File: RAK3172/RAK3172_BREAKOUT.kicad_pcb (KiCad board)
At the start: 2 copper layers, 29.4 x 36.8 mm, 5 parts, among them J1 Conn_01x14_Male, J2 Conn_01x14_Male, J3 Conn_01x14_Male, U1 RAK3172

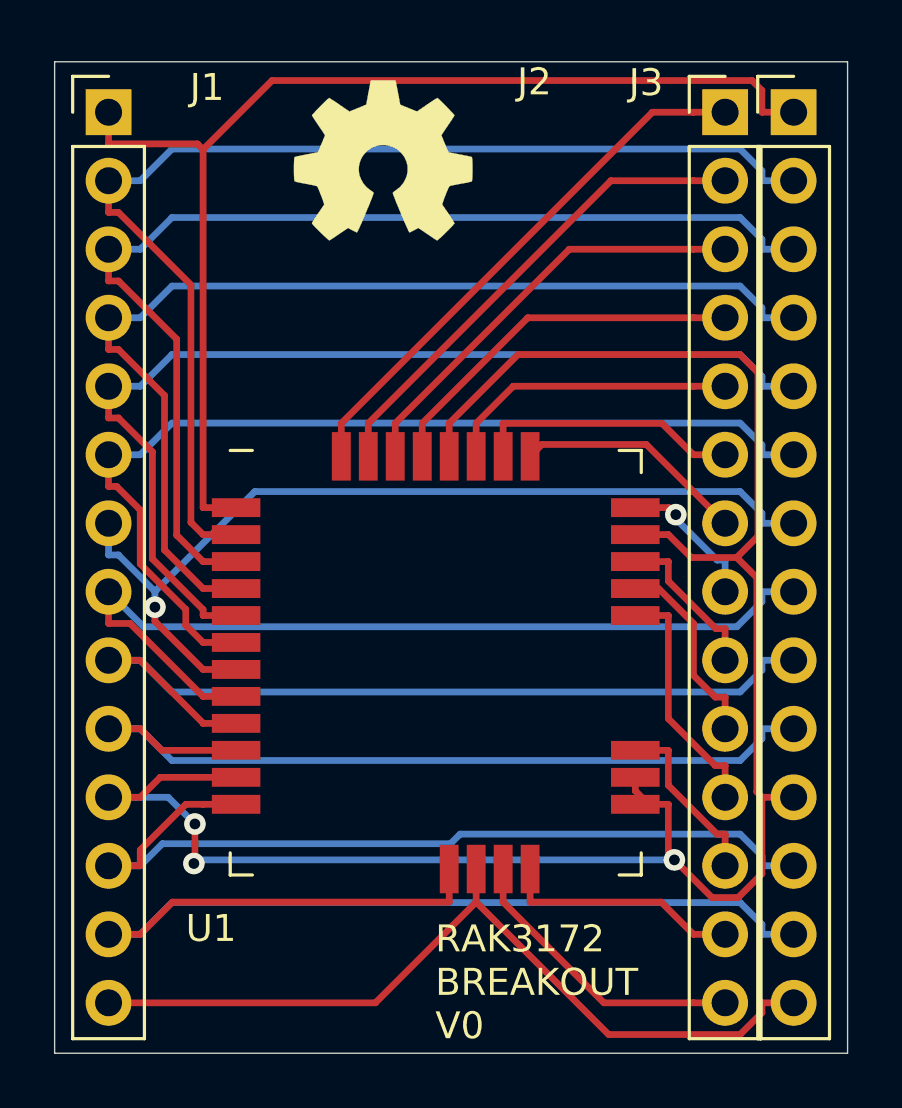
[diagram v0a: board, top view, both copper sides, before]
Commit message: pcb:(DIL_BREAKOUT_PCB RAK 3172) silks headers
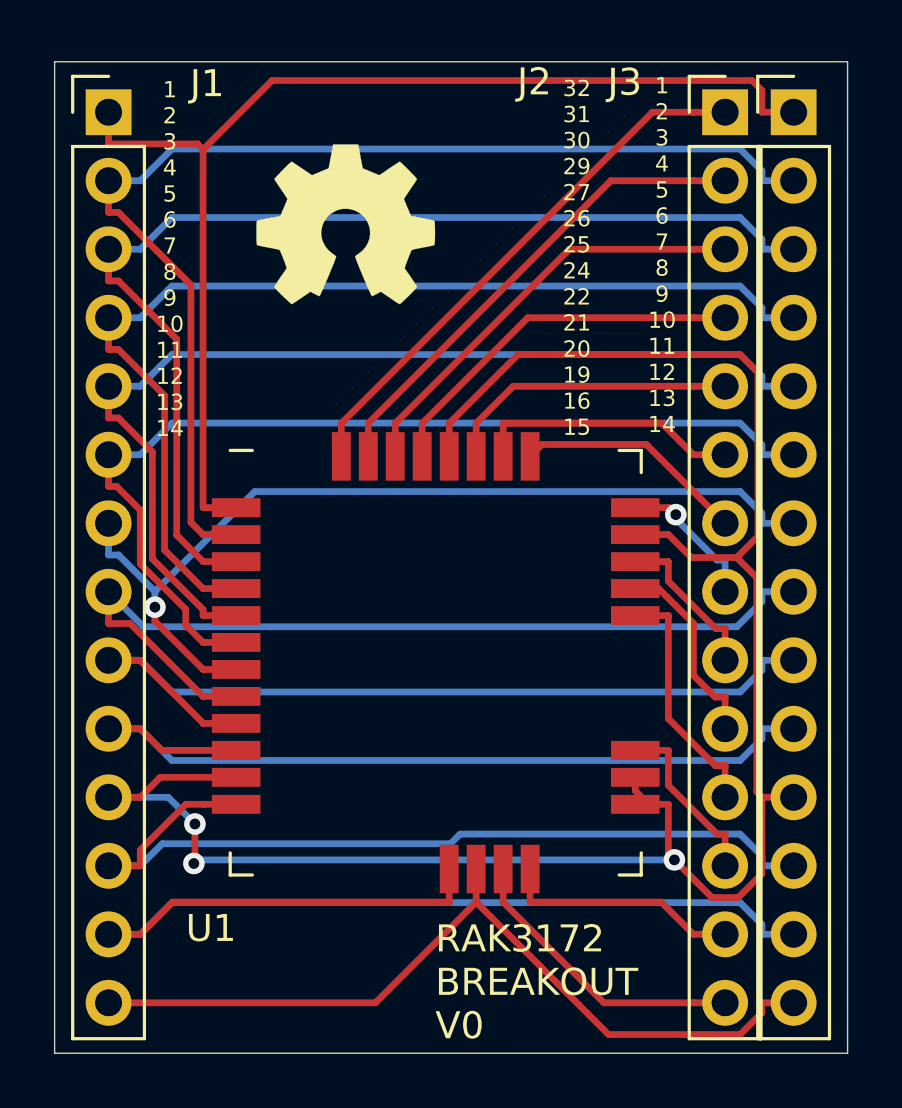
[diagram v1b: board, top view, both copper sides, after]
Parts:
- moved REF** 2.74 mm to (60.8, 56.0)
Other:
- board text added: "1 2 3 4 5 6 7 8 9 10 11 12 13 14"
- board text added: "32 31 30 29 27 26 25 24 22 21 20 19 16 15"
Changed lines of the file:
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@@
   (general
     (thickness 1.6)
-    (drawings 6)
+    (drawings 9)
     (tracks 244)
     (zones 0)
@@
     (descr "Through hole straight pin header, 1x14, 2.54mm pitch, single row")
     (tags "Through hole pin header THT 1x14 2.54mm single row")
-    (fp_text reference J3 (at -5.47228 -1.0954) (layer F.SilkS)
+    (fp_text reference J3 (at -6.25968 -1.11064) (layer F.SilkS)
       (effects (font (size 1 1) (thickness 0.15)))
     )
@@
     (descr "Through hole straight pin header, 1x14, 2.54mm pitch, single row")
     (tags "Through hole pin header THT 1x14 2.54mm single row")
-    (fp_text reference J1 (at 3.6514 -0.9176) (layer F.SilkS)
+    (fp_text reference J1 (at 3.65648 -1.05984) (layer F.SilkS)
       (effects (font (size 1 1) (thickness 0.15)))
     )
@@
   )
   (module Symbol:OSHW-Symbol_6.7x6mm_SilkScreen (layer F.Cu)
-    (at 62.17412 53.67528)
+    (at 60.7822 56.03748)
     (descr "Open Source Hardware Symbol")
     (tags "Logo Symbol OSHW")
@@
       (xy 0.555814 -2.531069)) (layer F.SilkS) (width 0.01))
   )
+  (gr_text "32\n31\n30\n29\n27\n26\n25\n24\n22\n21\n20\n19\n16\n15" (at 69.36232 57.27192) (layer F.SilkS)
+    (effects (font (size 0.6 0.6) (thickness 0.125)))
+  )
+  (gr_text "1\n2\n3\n4\n5\n6\n7\n8\n9\n10\n11\n12\n13\n14" (at 54.27472 57.31764) (layer F.SilkS)
+    (effects (font (size 0.6 0.6) (thickness 0.125)))
+  )
+  (gr_text "1\n2\n3\n4\n5\n6\n7\n8\n9\n10\n11\n12\n13\n14" (at 72.52208 57.17032) (layer F.SilkS)
+    (effects (font (size 0.6 0.6) (thickness 0.125)))
+  )
   (gr_text "RAK3172 \nBREAKOUT \nV0" (at 64.60236 84.0486) (layer B.SilkS)
